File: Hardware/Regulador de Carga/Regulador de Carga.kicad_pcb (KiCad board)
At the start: 2 copper layers, 16 parts, among them K1 DIPxx-1Cxx-51x

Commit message: regulador de carga (yeti)
es mi primer placa despues de años. ¿esta fachera, no?
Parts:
- removed K1: DIPxx-1Cxx-51x, Relay_THT:Relay_SPDT_Finder_36.11
- removed ZENER1: D_Zener, Diode_THT:D_A-405_P12.70mm_Horizontal
- added D2: D_Zener, Diode_THT:D_A-405_P12.70mm_Horizontal, F.Cu at (143.5, 82.5)
- added Q1: 2N3904, Package_TO_SOT_THT:TO-92_Inline, F.Cu at (157.5, 64.5)
- added R4: 0K, Resistor_THT:R_Axial_DIN0204_L3.6mm_D1.6mm_P7.62mm_Horizontal, F.Cu at (143.5, 67.0)
- moved C3 115.7 mm to (160.0, 77.5)
- moved op1 111.7 mm to (138.4, 78.7), turned to 180 degrees
- moved RV1 108.0 mm to (152.4, 81.3), turned to 180 degrees
- moved BATin1 100.7 mm to (123.2, 66.0), turned to 180 degrees
- moved R2 99.5 mm to (142.2, 86.4), turned to 180 degrees
- moved PANEL1 99.5 mm to (133.3, 65.0)
- moved C2 98.6 mm to (132.2, 82.5)
- moved LED1 97.6 mm to (156.2, 72.1)
- moved R3 95.3 mm to (151.1, 63.2), turned to 180 degrees
- moved C1 88.4 mm to (122.0, 81.0), turned to 180 degrees
- moved R1 87.6 mm to (128.0, 70.6), turned to 90 degrees
- moved BATout1 86.3 mm to (110.5, 64.8)
- moved LM7805 86.0 mm to (118.1, 76.2), turned to 0 degrees
- moved D1 73.5 mm to (113.0, 85.1)
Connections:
- D1 pad 1: Net-(D1-Pad1) -> (no net)
- D1 pad 2: Net-(D1-Pad2) -> Net-(BATin1-Pad2)
- PANEL1 pad 2: Net-(D1-Pad1) -> Net-(PANEL1-Pad2)
- R3 pad 1: Net-(K1-Pad6) -> Net-(Q1-Pad3)
- R3 pad 2: Net-(LED1-Pad2) -> Net-(PANEL1-Pad2)
- op1 pad 6: Net-(K1-Pad6) -> (no net)
- op1 pad 7: Net-(BATin1-Pad2) -> Net-(PANEL1-Pad2)
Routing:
- net Net-(K1-Pad6): track 72.5 -> 0.00 mm
- net Net-(PANEL1-Pad2): track 0.00 -> 69.7 mm
- net (no net): track 0.00 -> 51.3 mm
- net Net-(BATin1-Pad2): track 87.3 -> 47.5 mm
- net Net-(C2-Pad1): track 15.4 -> 36.2 mm
- net Net-(D1-Pad2): track 12.0 -> 0.00 mm
- net Net-(Q1-Pad2): track 0.00 -> 7.16 mm
- net Net-(C3-Pad2): track 19.6 -> 25.1 mm
- net Earth: track 0.00 -> 5.36 mm, vias 0 -> 2
- net Net-(D1-Pad1): track 5.08 -> 0.00 mm
- net Net-(Q1-Pad3): track 0.00 -> 4.34 mm
- net Net-(D2-Pad2): track 0.00 -> 2.81 mm
- net Net-(R2-Pad1): track 9.57 -> 12.3 mm
- net Net-(LED1-Pad2): track 5.50 -> 8.15 mm
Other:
- board outline added: 56 x 30 mm

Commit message: PCB regulador de carga
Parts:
- added D3: DIODE, Diode_THT:D_A-405_P12.70mm_Horizontal, F.Cu at (143.3, 78.0)
- added D4: DIODE, Diode_THT:D_A-405_P12.70mm_Horizontal, F.Cu at (156.0, 74.2)
- added D5: DIODE, Diode_THT:D_A-405_P12.70mm_Horizontal, F.Cu at (143.3, 70.1)
- D2: value D_Zener -> DIODE
- R3: value 1K -> 220
- R4: value 0K -> 220
- moved RV1 12.7 mm to (165.1, 80.8)
- moved D2 12.4 mm to (156.0, 82.3), turned to 180 degrees
- moved LED1 9.55 mm to (163.6, 66.0), turned to 90 degrees
- moved C3 8.41 mm to (164.1, 84.8)
- moved R4 7.94 mm to (151.4, 66.0), turned to 180 degrees
- moved R2 1.61 mm to (140.7, 85.9)
- moved Q1 0.72 mm to (158.0, 64.0)
- moved R3 0.72 mm to (151.6, 62.7)
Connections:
- D1 pad 1: (no net) -> Net-(D1-Pad1)
- R4 pad 1: Net-(D2-Pad2) -> Net-(Q1-Pad2)
- R4 pad 2: Net-(Q1-Pad2) -> Net-(D5-Pad2)
- op1 pad 2: Net-(C3-Pad2) -> Net-(op1-Pad2)
- op1 pad 6: (no net) -> Net-(D1-Pad1)
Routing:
- net (no net): track 51.3 -> 0.00 mm
- net Net-(D1-Pad1): track 0.00 -> 46.5 mm
- net Net-(PANEL1-Pad2): track 69.7 -> 34.5 mm
- net Net-(D5-Pad2): track 0.00 -> 13.9 mm
- net Net-(C3-Pad2): track 25.1 -> 12.4 mm
- net Net-(R2-Pad1): track 12.3 -> 0.00 mm
- net Net-(LED1-Pad2): track 8.15 -> 0.00 mm
- net Net-(D4-Pad2): track 0.00 -> 4.06 mm
- net Net-(D3-Pad2): track 0.00 -> 3.88 mm
- net Net-(BATin1-Pad2): track 47.5 -> 45.8 mm
- net Net-(D2-Pad2): track 2.81 -> 4.25 mm
- removed copper zone on B.Cu, net Earth

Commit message: Actualice el PCB del regulador de carga
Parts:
- removed D3, D4, D5: DIODE, Diode_THT:D_A-405_P12.70mm_Horizontal
- removed LED1: LED, LED_THT:LED_D5.0mm
- removed Q1: 2N3904, Package_TO_SOT_THT:TO-92_Inline
- removed R4: 220, Resistor_THT:R_Axial_DIN0204_L3.6mm_D1.6mm_P7.62mm_Horizontal
- added op2: OP07, Package_DIP:DIP-8_W7.62mm, F.Cu at (152.9, 78.7)
- D2: value DIODE -> LED; footprint Diode_THT:D_A-405_P12.70mm_Horizontal -> LED_THT:LED_D3.0mm
- R3: value 220 -> 1.2K
- moved C3 29.5 mm to (134.7, 82.8), turned to 0 degrees
- moved RV1 22.2 mm to (143.8, 87.3), turned to 90 degrees
- moved D2 21.4 mm to (145.8, 63.5), turned to 0 degrees
- moved C2 6.14 mm to (126.1, 81.8)
- moved R3 4.85 mm to (151.9, 67.6)
- moved R2 3.59 mm to (137.2, 85.3)
- moved BATin1 1.02 mm to (123.2, 65.0)
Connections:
- D2 pad 1: Net-(C3-Pad2) -> Earth
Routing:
- net Net-(D5-Pad2): track 13.9 -> 0.00 mm
- net Net-(D1-Pad1): track 46.5 -> 33.9 mm
- net Net-(C3-Pad2): track 12.4 -> 20.3 mm
- net Net-(R3-Pad1): track 4.34 -> 12.0 mm
- net Net-(R2-Pad1): track 0.00 -> 7.56 mm
- net Net-(BATin1-Pad2): track 45.8 -> 38.5 mm
- net Net-(C2-Pad1): track 36.2 -> 29.0 mm
- net Net-(D2-Pad2): track 4.25 -> 11.4 mm
- net Net-(Q1-Pad2): track 6.91 -> 0.00 mm
- net Net-(D4-Pad2): track 4.06 -> 0.00 mm
- net Net-(D3-Pad2): track 3.88 -> 0.00 mm
- net Net-(PANEL1-Pad2): track 34.5 -> 31.5 mm
- net Earth: vias 2 -> 1
- added copper zone on B.Cu, net Earth

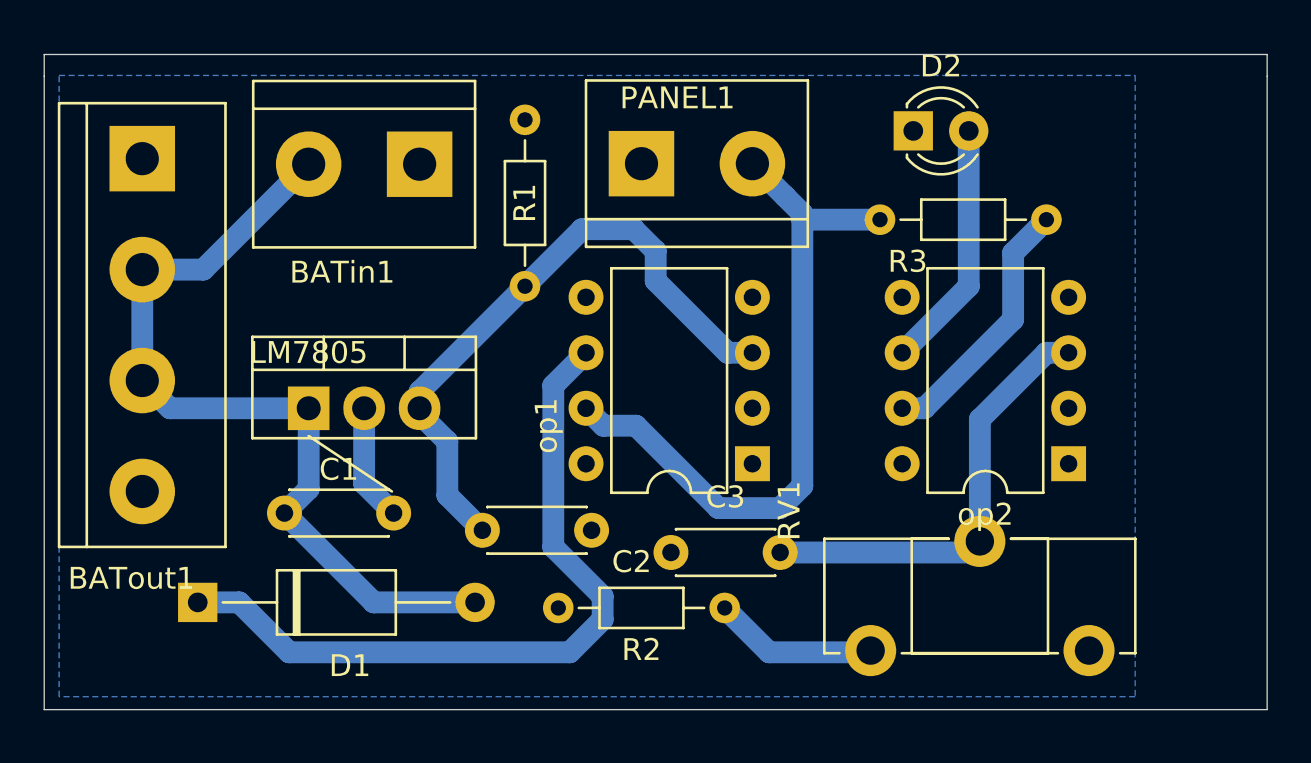
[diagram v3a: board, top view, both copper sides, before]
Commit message: Corregir errores del RC
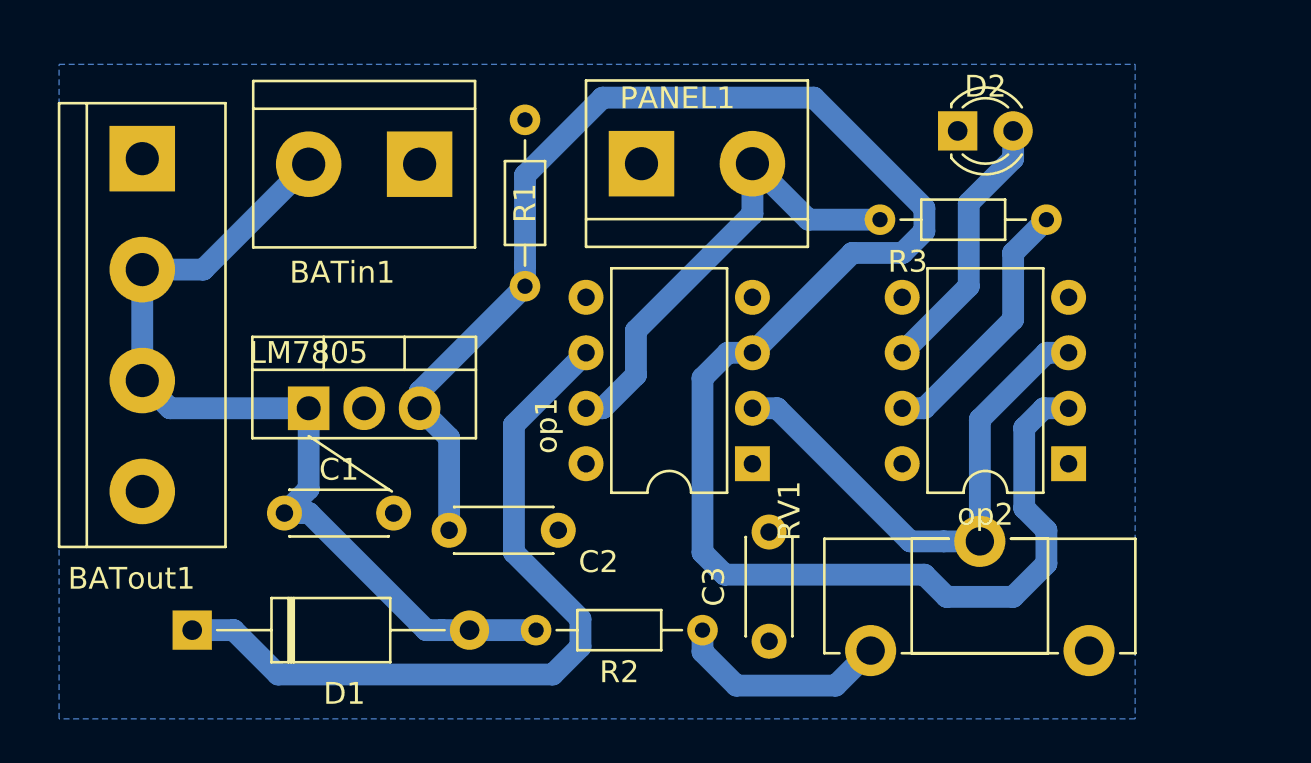
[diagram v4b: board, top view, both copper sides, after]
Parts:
- moved C3 6.06 mm to (139.2, 86.9), turned to 90 degrees
- moved D2 2.03 mm to (147.8, 63.5)
- moved C2 1.52 mm to (124.5, 81.8)
- moved R2 1.44 mm to (136.1, 86.4)
- moved D1 1.30 mm to (112.8, 86.4)
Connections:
- op1 pad 2: Net-(op1-Pad2) -> Net-(C3-Pad2)
- op2 pad 2: Net-(op2-Pad2) -> Net-(C2-Pad1)
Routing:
- net Net-(C2-Pad1): track 29.0 -> 88.9 mm
- net Net-(PANEL1-Pad2): track 31.5 -> 21.7 mm
- net Earth: track 5.36 -> 0.00 mm
- net Net-(C3-Pad2): track 20.3 -> 23.9 mm
- net Net-(BATin1-Pad2): track 38.5 -> 41.8 mm
- net Net-(R2-Pad1): track 7.56 -> 10.00 mm
- net Net-(D1-Pad1): track 33.9 -> 35.2 mm
- net Net-(D2-Pad2): track 11.4 -> 12.3 mm
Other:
- board outline removed

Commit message: Actualizar el PCB
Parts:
- removed op2: OP07, Package_DIP:DIP-8_W7.62mm
- added QN1: IRF540N, Package_TO_SOT_THT:TO-220-3_Vertical, F.Cu at (144.3, 77.7)
- added QP1: IRF9540N, Package_TO_SOT_THT:TO-220-3_Vertical, F.Cu at (144.3, 71.6)
- D1: value DIODE -> D_Zener; footprint Diode_THT:D_A-405_P12.70mm_Horizontal -> Diode_THT:D_DO-15_P12.70mm_Horizontal
- moved D1 38.7 mm to (143.3, 62.5)
- moved D2 13.2 mm to (154.9, 74.7), turned to 90 degrees
- moved op1 10.3 mm to (131.6, 71.1), turned to 0 degrees
- moved R3 2.74 mm to (154.4, 66.5)
- moved R1 2.54 mm to (128.0, 73.2)
- moved BATout1 1.78 mm to (110.5, 66.5)
- moved C3 1.44 mm to (139.2, 88.3)
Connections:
- D1 pad 1: Net-(D1-Pad1) -> Net-(BATin1-Pad2)
- D1 pad 2: Net-(BATin1-Pad2) -> Net-(D1-Pad2)
- R3 pad 1: Net-(R3-Pad1) -> Net-(D2-Pad2)
- R3 pad 2: Net-(PANEL1-Pad2) -> Net-(QP1-Pad2)
- op1 pad 6: Net-(D1-Pad1) -> Net-(QN1-Pad1)
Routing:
- net Net-(C2-Pad1): track 88.9 -> 19.9 mm
- net Net-(D1-Pad1): track 35.2 -> 0.00 mm
- net Net-(BATin1-Pad2): track 41.8 -> 69.2 mm
- net Net-(D1-Pad2): track 0.00 -> 19.2 mm
- net Net-(PANEL1-Pad2): track 21.7 -> 38.8 mm
- net Net-(R3-Pad1): track 12.0 -> 0.00 mm
- net Net-(QN1-Pad1): track 0.00 -> 11.8 mm
- net Net-(D2-Pad2): track 12.3 -> 5.80 mm
- net Net-(QP1-Pad2): track 0.00 -> 5.08 mm
- net Net-(R2-Pad1): track 10.00 -> 8.93 mm
- net Net-(op1-Pad8): vias 0 -> 1
- net Earth: vias 1 -> 0

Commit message: Detalles del PCB
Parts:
- moved D1 0.51 mm to (143.3, 63.0)
- moved D2 0.51 mm to (154.9, 75.2)
- moved QN1 0.51 mm to (144.3, 78.2)
- moved QP1 0.51 mm to (144.3, 72.1)
- moved R3 0.51 mm to (154.4, 67.1)
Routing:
- net Net-(BATin1-Pad2): track 69.2 -> 70.1 mm
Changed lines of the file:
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@@
     (thickness 1.6)
     (drawings 1)
-    (tracks 58)
+    (tracks 59)
     (zones 0)
     (modules 16)
@@
   )
   (module Diode_THT:D_DO-15_P12.70mm_Horizontal (layer F.Cu)
-    (at 143.256 62.484)
+    (at 143.256 62.992)
     (descr "Diode, DO-15 series, Axial, Horizontal, pin pitch=12.7mm, , length*diameter=7.6*3.6mm^2, , http://www.diodes.com/_files/packages/DO-15.pdf")
     (tags "Diode DO-15 series Axial Horizontal pin pitch 12.7mm  length 7.6mm diameter 3.6mm")
@@
       (effects (font (size 1 1) (thickness 0.15)))
     )
-    (fp_text user K (at 0 -2.2) (layer F.SilkS)
-      (effects (font (size 1 1) (thickness 0.15)))
-    )
-    (fp_text user K (at 0 -2.2) (layer F.Fab)
+    (fp_text user K (at 0 -1.778) (layer F.SilkS)
+      (effects (font (size 1 1) (thickness 0.15)))
+    )
+    (fp_text user K (at 0 -1.778) (layer F.Fab)
       (effects (font (size 1 1) (thickness 0.15)))
     )
@@
   )
   (module Resistor_THT:R_Axial_DIN0204_L3.6mm_D1.6mm_P7.62mm_Horizontal (layer F.Cu)
-    (at 154.432 66.548 180)
+    (at 154.432 67.056 180)
     (descr "Resistor, Axial_DIN0204 series, Axial, Horizontal, pin pitch=7.62mm, 0.167W, length*diameter=3.6*1.6mm^2, http://cdn-reichelt.de/documents/datenblatt/B400/1_4W%23YAG.pdf")
     (tags "Resistor Axial_DIN0204 series Axial Horizontal pin pitch 7.62mm 0.167W length 3.6mm diameter 1.6mm")
@@
   )
   (module Package_TO_SOT_THT:TO-220-3_Vertical (layer F.Cu)
-    (at 144.272 71.628)
+    (at 144.272 72.136)
     (descr "TO-220-3, Vertical, RM 2.54mm, see https://www.vishay.com/docs/66542/to-220-1.pdf")
     (tags "TO-220-3 Vertical RM 2.54mm")
@@
   )
   (module Package_TO_SOT_THT:TO-220-3_Vertical (layer F.Cu)
-    (at 144.272 77.724)
+    (at 144.272 78.232)
     (descr "TO-220-3, Vertical, RM 2.54mm, see https://www.vishay.com/docs/66542/to-220-1.pdf")
     (tags "TO-220-3 Vertical RM 2.54mm")
@@
   )
   (module LED_THT:LED_D3.0mm (layer F.Cu)
-    (at 154.94 74.676 90)
+    (at 154.94 75.184 90)
     (descr "LED, diameter 3.0mm, 2 pins")
     (tags "LED diameter 3.0mm 2 pins")
@@
   (segment (start 110.49 71.628) (end 111.76 71.628) (width 1) (layer B.Cu) (net 1))
   (segment (start 111.76 71.628) (end 118.11 65.278) (width 1) (layer B.Cu) (net 1))
-  (segment (start 142.748 61.976) (end 143.256 62.484) (width 1) (layer B.Cu) (net 1))
-  (segment (start 120.904 61.976) (end 142.748 61.976) (width 1) (layer B.Cu) (net 1))
+  (segment (start 142.748 62.484) (end 143.256 62.992) (width 1) (layer B.Cu) (net 1))
+  (segment (start 142.24 61.976) (end 143.256 62.992) (width 1) (layer B.Cu) (net 1))
+  (segment (start 120.904 61.976) (end 142.24 61.976) (width 1) (layer B.Cu) (net 1))
   (segment (start 118.11 65.024) (end 118.11 64.77) (width 1) (layer B.Cu) (net 1))
   (segment (start 118.11 64.77) (end 120.904 61.976) (width 1) (layer B.Cu) (net 1))
@@
   (segment (start 134.62 79.87137) (end 138.06063 83.312) (width 1) (layer B.Cu) (net 4))
   (segment (start 138.06063 83.312) (end 139.192 83.312) (width 1) (layer B.Cu) (net 4))
-  (segment (start 154.432 71.628) (end 154.94 72.136) (width 1) (layer B.Cu) (net 8))
-  (segment (start 154.432 66.548) (end 154.432 71.628) (width 1) (layer B.Cu) (net 8))
-  (segment (start 148.844 72.136) (end 149.352 71.628) (width 1) (layer B.Cu) (net 9))
-  (segment (start 148.844 74.676) (end 148.844 72.136) (width 1) (layer B.Cu) (net 9))
-  (segment (start 146.812 77.724) (end 146.812 76.708) (width 1) (layer B.Cu) (net 9))
-  (segment (start 146.812 76.708) (end 148.844 74.676) (width 1) (layer B.Cu) (net 9))
+  (segment (start 154.432 72.136) (end 154.94 72.644) (width 1) (layer B.Cu) (net 8))
+  (segment (start 154.432 67.056) (end 154.432 72.136) (width 1) (layer B.Cu) (net 8))
+  (segment (start 148.844 72.644) (end 149.352 72.136) (width 1) (layer B.Cu) (net 9))
+  (segment (start 148.844 75.184) (end 148.844 72.644) (width 1) (layer B.Cu) (net 9))
+  (segment (start 146.812 78.232) (end 146.812 77.216) (width 1) (layer B.Cu) (net 9))
+  (segment (start 146.812 77.216) (end 148.844 75.184) (width 1) (layer B.Cu) (net 9))
   (segment (start 138.176 73.66) (end 139.192 73.66) (width 1) (layer B.Cu) (net 9))
   (segment (start 136.652 72.136) (end 138.176 73.66) (width 1) (layer B.Cu) (net 9))
   (segment (start 138.43 65) (end 136.652 66.778) (width 1) (layer B.Cu) (net 9))
   (segment (start 136.652 66.778) (end 136.652 72.136) (width 1) (layer B.Cu) (net 9))
-  (segment (start 137.668 80.772) (end 145.764 80.772) (width 1) (layer B.Cu) (net 9))
-  (segment (start 146.812 79.724) (end 146.812 77.724) (width 1) (layer B.Cu) (net 9))
-  (segment (start 136.144 79.248) (end 137.668 80.772) (width 1) (layer B.Cu) (net 9))
-  (segment (start 145.764 80.772) (end 146.812 79.724) (width 1) (layer B.Cu) (net 9))
+  (segment (start 136.144 79.248) (end 138.176 81.28) (width 1) (layer B.Cu) (net 9))
   (segment (start 139.192 73.66) (end 136.144 76.708) (width 1) (layer B.Cu) (net 9))
+  (segment (start 138.176 81.28) (end 145.796 81.28) (width 1) (layer B.Cu) (net 9))
   (segment (start 136.144 76.708) (end 136.144 79.248) (width 1) (layer B.Cu) (net 9))
+  (segment (start 146.812 80.264) (end 146.812 78.232) (width 1) (layer B.Cu) (net 9))
+  (segment (start 145.796 81.28) (end 146.812 80.264) (width 1) (layer B.Cu) (net 9))
   (segment (start 141.892 85.344) (end 143.844 87.296) (width 1) (layer B.Cu) (net 10))
   (segment (start 136.144 86.36) (end 137.16 85.344) (width 1) (layer B.Cu) (net 10))
   (segment (start 137.16 85.344) (end 141.892 85.344) (width 1) (layer B.Cu) (net 10))
-  (segment (start 153.924 62.484) (end 155.956 62.484) (width 1) (layer B.Cu) (net 11))
-  (segment (start 151.892 64.516) (end 153.924 62.484) (width 1) (layer B.Cu) (net 11))
-  (segment (start 151.892 75.1365) (end 151.892 64.516) (width 1) (layer B.Cu) (net 11))
-  (segment (start 149.352 77.724) (end 149.352 77.6765) (width 1) (layer B.Cu) (net 11))
-  (segment (start 149.352 77.6765) (end 151.892 75.1365) (width 1) (layer B.Cu) (net 11))
-  (segment (start 144.272 71.628) (end 144.272 77.724) (width 1) (layer B.Cu) (net 12))
-  (segment (start 142.748 76.2) (end 144.272 77.724) (width 1) (layer B.Cu) (net 12))
-  (segment (start 139.192 76.2) (end 142.748 76.2) (width 1) (layer B.Cu) (net 12))
-  (segment (start 146.812 71.628) (end 146.812 66.548) (width 1) (layer B.Cu) (net 13))
+  (segment (start 151.892 75.6445) (end 151.892 65.024) (width 1) (layer B.Cu) (net 11))
+  (segment (start 149.352 78.232) (end 149.352 78.1845) (width 1) (layer B.Cu) (net 11))
+  (segment (start 149.352 78.1845) (end 151.892 75.6445) (width 1) (layer B.Cu) (net 11))
+  (segment (start 151.892 65.024) (end 153.924 62.992) (width 1) (layer B.Cu) (net 11))
+  (segment (start 153.924 62.992) (end 155.956 62.992) (width 1) (layer B.Cu) (net 11))
+  (segment (start 144.272 72.136) (end 144.272 78.232) (width 1) (layer B.Cu) (net 12))
+  (segment (start 142.24 76.2) (end 144.272 78.232) (width 1) (layer B.Cu) (net 12))
+  (segment (start 139.192 76.2) (end 142.24 76.2) (width 1) (layer B.Cu) (net 12))
+  (segment (start 146.812 72.136) (end 146.812 67.056) (width 1) (layer B.Cu) (net 13))
   (zone (net 2) (net_name Earth) (layer B.Cu) (hatch edge 0.508)
     (connect_pads (clearance 0.508))
